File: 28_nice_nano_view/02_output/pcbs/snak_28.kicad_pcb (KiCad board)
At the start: 2 copper layers, 114.8 x 99.6 mm, 172 parts

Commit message: test trackpoint footprints
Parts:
- moved TP1 1.25 mm to (172.8, 62.4), turned to 0 degrees
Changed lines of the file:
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@@
         )
       (module trackpoint_mount_t430 (layer F.Cu)
-        (at 174 62.35 90)
+        (at 172.75 62.35 0)
         (attr virtual)
         (fp_text reference "TP1" (at 0 0) (layer B.SilkS) hide
@@
 (gr_circle (center 170.43886559999999 124.35568) (end 171.43886559999999 124.35568) (layer Eco1.User) (width 0.15))
 (gr_circle (center 201.925 53.975) (end 202.925 53.975) (layer Eco1.User) (width 0.15))
-(gr_circle (center 174 52.85) (end 175 52.85) (layer Eco1.User) (width 0.15))
-(gr_circle (center 174 71.85) (end 175 71.85) (layer Eco1.User) (width 0.15))
+(gr_circle (center 172.75 52.85) (end 173.75 52.85) (layer Eco1.User) (width 0.15))
+(gr_circle (center 172.75 71.85) (end 173.75 71.85) (layer Eco1.User) (width 0.15))
 (gr_line (start 93.05 89.45) (end 106.95 89.45) (angle 90) (layer Eco1.User) (width 0.15))
 (gr_line (start 106.95 89.45) (end 106.95 75.55) (angle 90) (layer Eco1.User) (width 0.15))
@@
 (gr_circle (center 170.43886559999999 124.35568) (end 171.93886559999999 124.35568) (layer Eco2.User) (width 0.15))
 (gr_circle (center 201.925 53.975) (end 203.425 53.975) (layer Eco2.User) (width 0.15))
-(gr_circle (center 174 52.85) (end 175.5 52.85) (layer Eco2.User) (width 0.15))
-(gr_circle (center 174 71.85) (end 175.5 71.85) (layer Eco2.User) (width 0.15))
+(gr_circle (center 172.75 52.85) (end 174.25 52.85) (layer Eco2.User) (width 0.15))
+(gr_circle (center 172.75 71.85) (end 174.25 71.85) (layer Eco2.User) (width 0.15))
 )

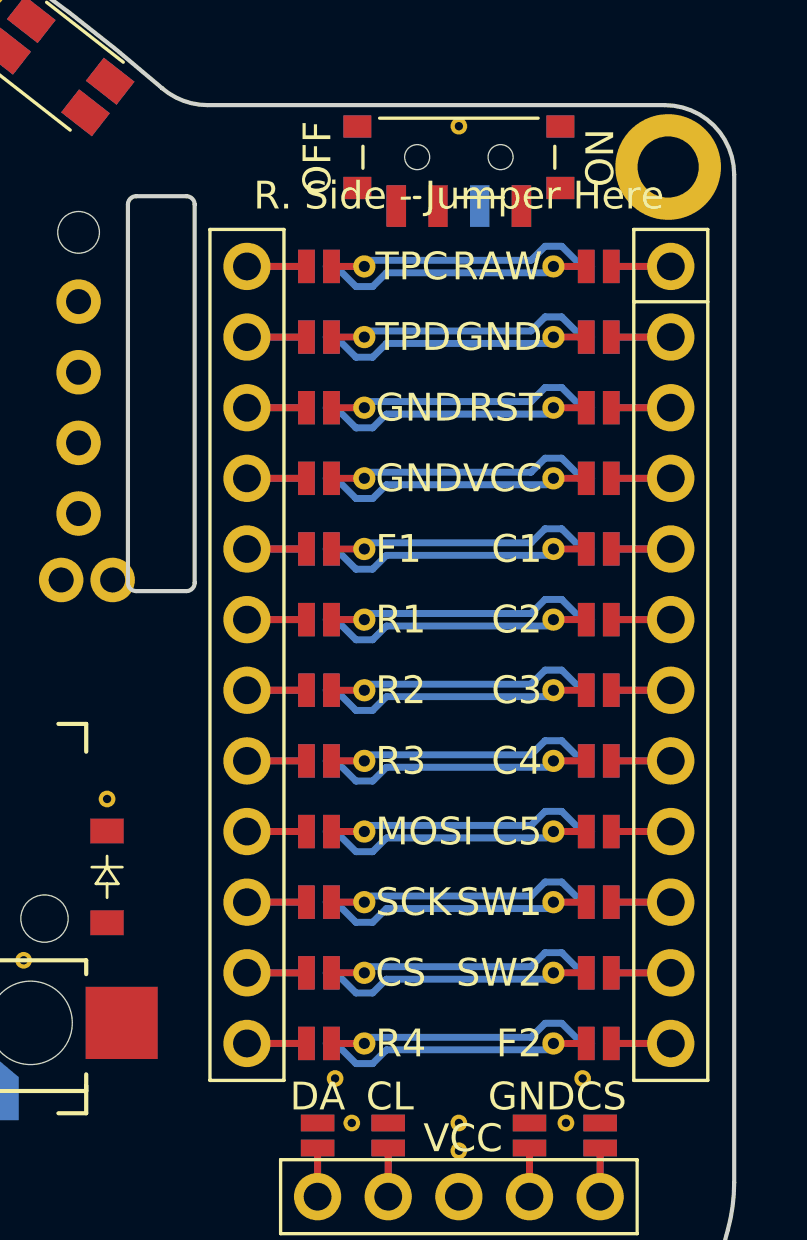
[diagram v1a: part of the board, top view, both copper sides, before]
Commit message: add cli config
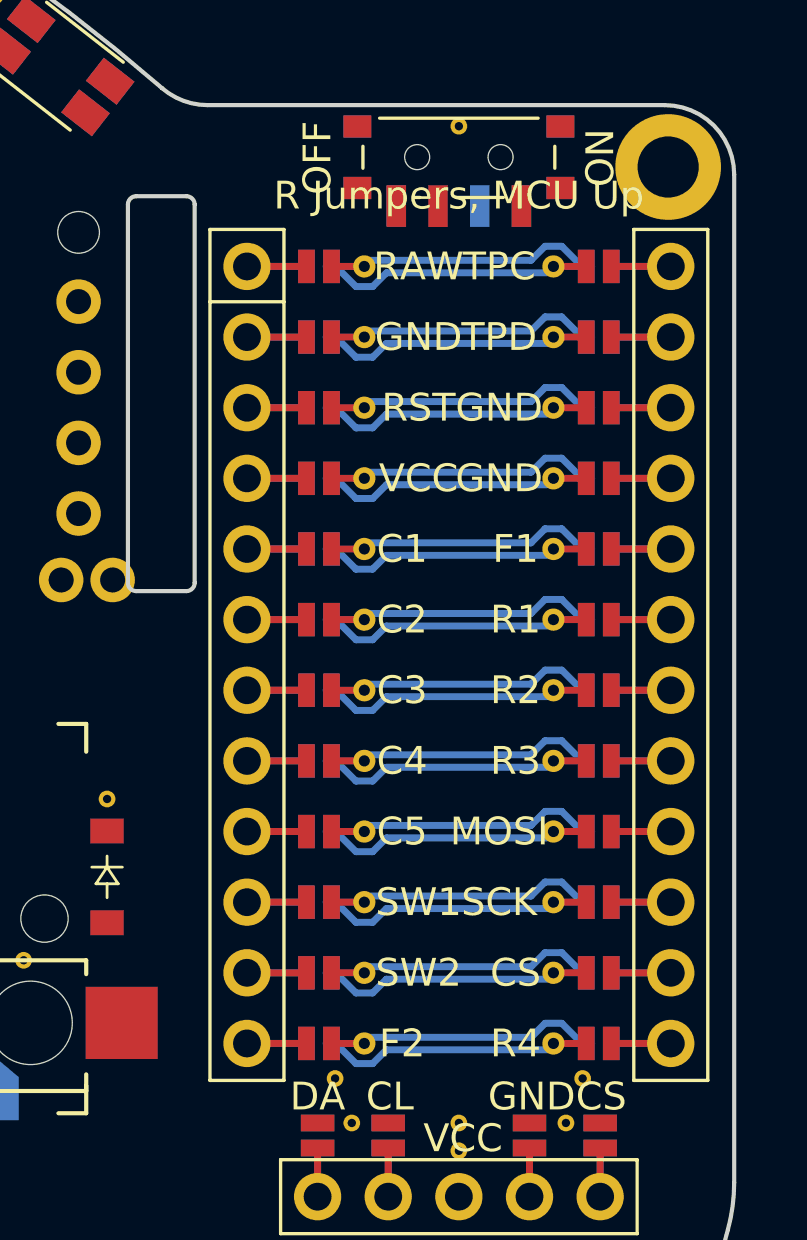
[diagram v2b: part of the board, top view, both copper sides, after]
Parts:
- MCU1: footprint ceoloide:nice_nano -> ceoloide:mcu_nice_nano
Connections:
- MCU1 pad 1: RAW -> MCU1_1
- MCU1 pad 10: SW1 -> MCU1_10
- MCU1 pad 11: SW2 -> MCU1_11
- MCU1 pad 113: R4 -> F2
- MCU1 pad 114: CS -> SW2
- MCU1 pad 115: SCK -> SW1
- MCU1 pad 116: MOSI -> C5
- MCU1 pad 117: R3 -> C4
- MCU1 pad 118: R2 -> C3
- MCU1 pad 119: R1 -> C2
- MCU1 pad 12: F2 -> MCU1_12
- MCU1 pad 120: F1 -> C1
- MCU1 pad 121: GND -> VCC
- MCU1 pad 122: GND -> RST
- MCU1 pad 123: TPD -> GND
- MCU1 pad 124: TPC -> RAW
- MCU1 pad 2: GND -> MCU1_2
- MCU1 pad 3: RST -> MCU1_3
- MCU1 pad 4: VCC -> MCU1_4
- MCU1 pad 5: C1 -> MCU1_5
- MCU1 pad 6: C2 -> MCU1_6
- MCU1 pad 7: C3 -> MCU1_7
- MCU1 pad 8: C4 -> MCU1_8
- MCU1 pad 9: C5 -> MCU1_9
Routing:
- net (no net): track 0.00 -> 333.1 mm
- net R2: track 101.6 -> 0.00 mm
- net pinky_mid: track 101.4 -> 0.00 mm
- net RAW: track 50.9 -> 0.00 mm
- net R4: track 50.9 -> 0.00 mm
- net index_bot: track 14.2 -> 0.00 mm
- net C1: track 14.2 -> 0.00 mm
